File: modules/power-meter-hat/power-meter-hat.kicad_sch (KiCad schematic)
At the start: 14 parts, among them J1 GPIO, U1 CAT24C256

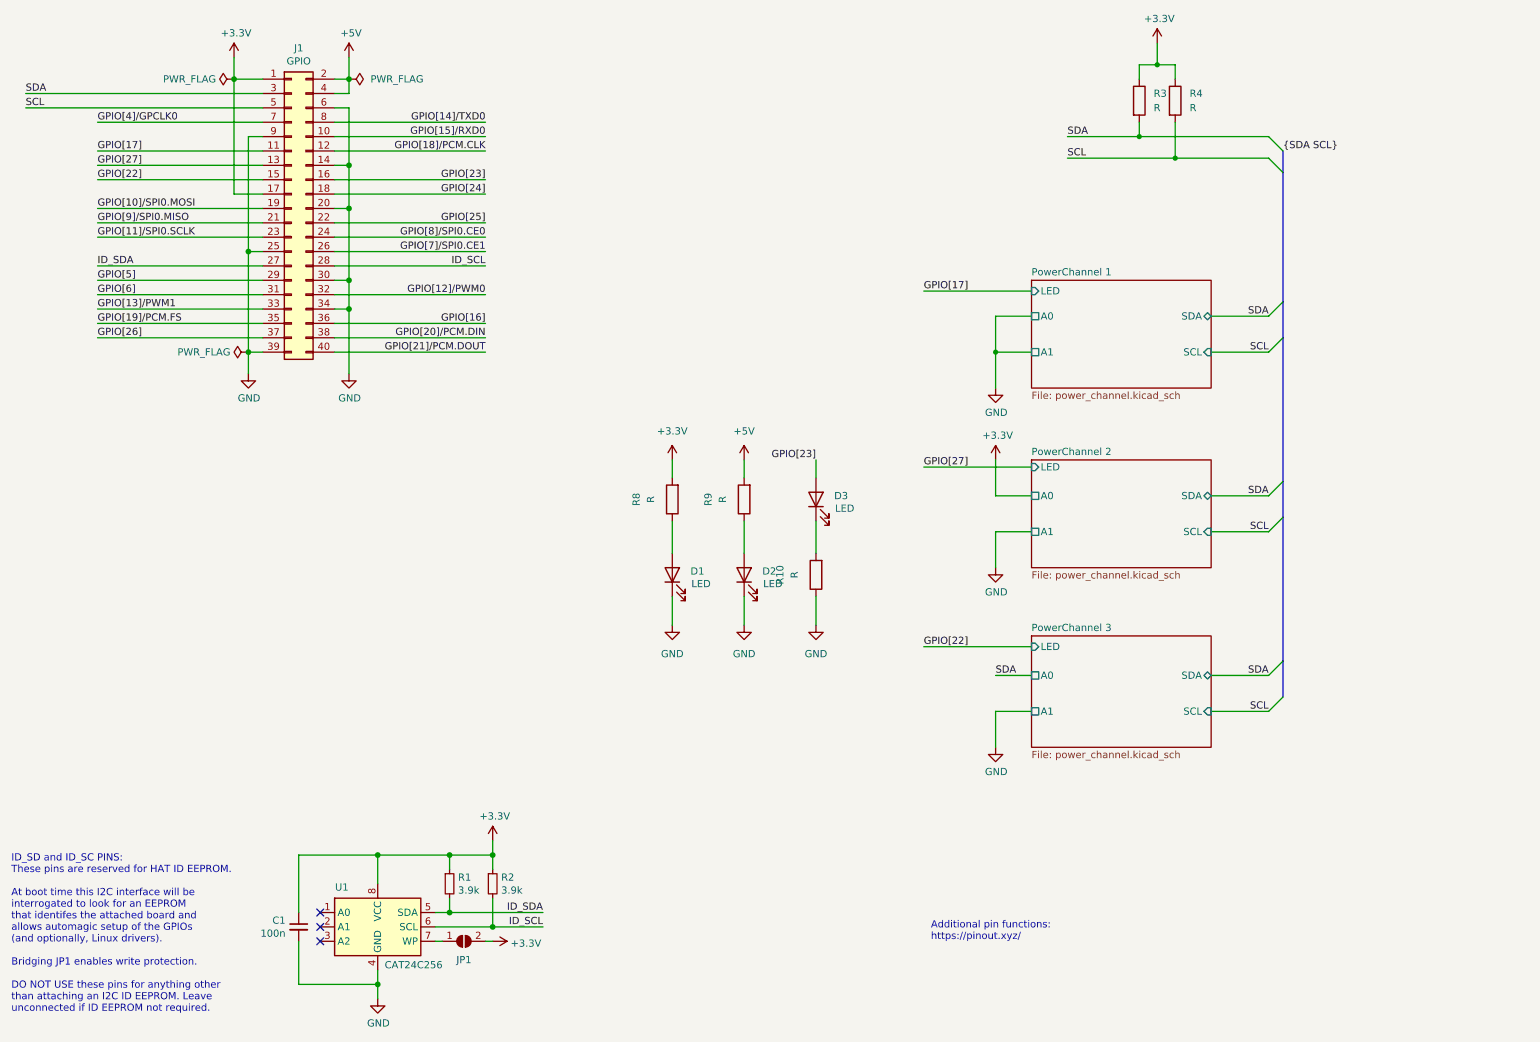
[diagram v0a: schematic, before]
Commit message: Add external power source
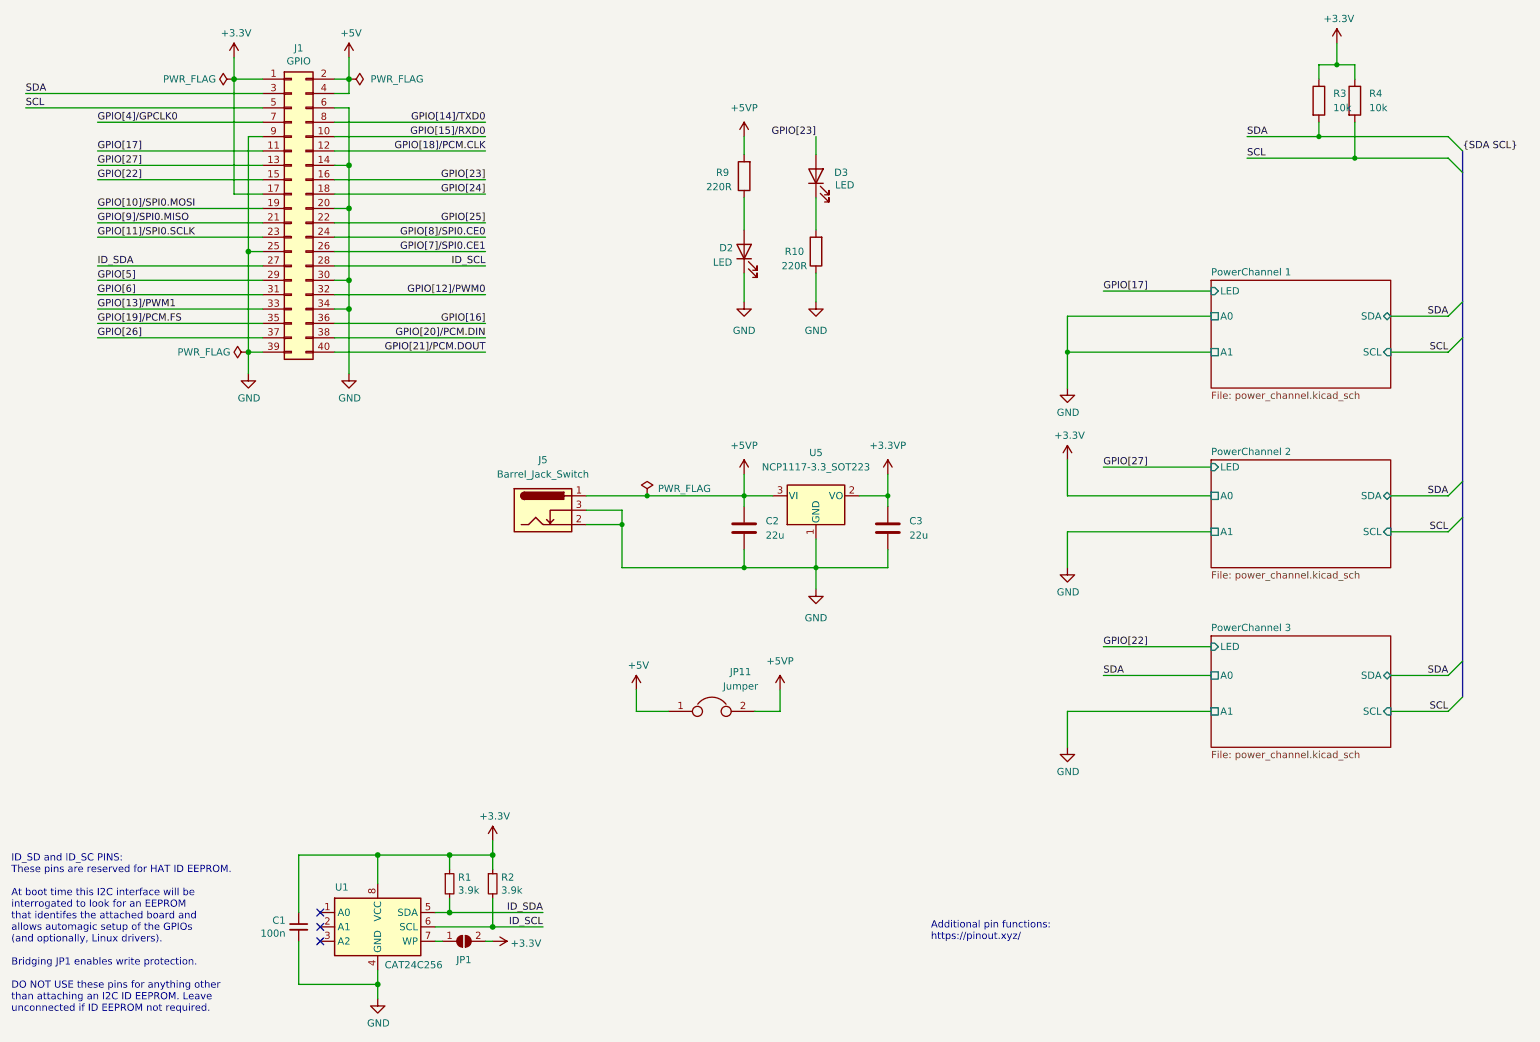
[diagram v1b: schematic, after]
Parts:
- removed D1: LED, LED_SMD:LED_1206_3216Metric_Castellated, symbol Device:LED
- removed R8: R, Resistor_SMD:R_0805_2012Metric_Pad1.20x1.40mm_HandSolder, symbol Device:R
- added C2, C3: 22u, Capacitor_SMD:C_0805_2012Metric_Pad1.18x1.45mm_HandSolder, symbol Device:C
- added J5: Barrel_Jack_Switch, Connector_BarrelJack:BarrelJack_Wuerth_6941xx301002, symbol Connector:Barrel_Jack_Switch
- added JP11: Jumper, Jumper:SolderJumper-2_P1.3mm_Open_TrianglePad1.0x1.5mm, symbol Device:Jumper
- added U5: NCP1117-3.3_SOT223, Package_TO_SOT_SMD:SOT-223-3_TabPin2, symbol Regulator_Linear:NCP1117-3.3_SOT223
- R10, R9: value R -> 220R
- R3, R4: value R -> 10k
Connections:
- net +5V: now also JP11.1; no longer R9.2
- net GND: now also C2.2, C3.2, J5.2, J5.3, U5.1 (GND)
- new net +3.3VP: C3.1, U5.2 (VO)
- new net +5VP: C2.1, J5.1, JP11.2, R9.2, U5.3 (VI)
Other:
- moved on the sheet: D2, D3, R10, R3, R4, R9

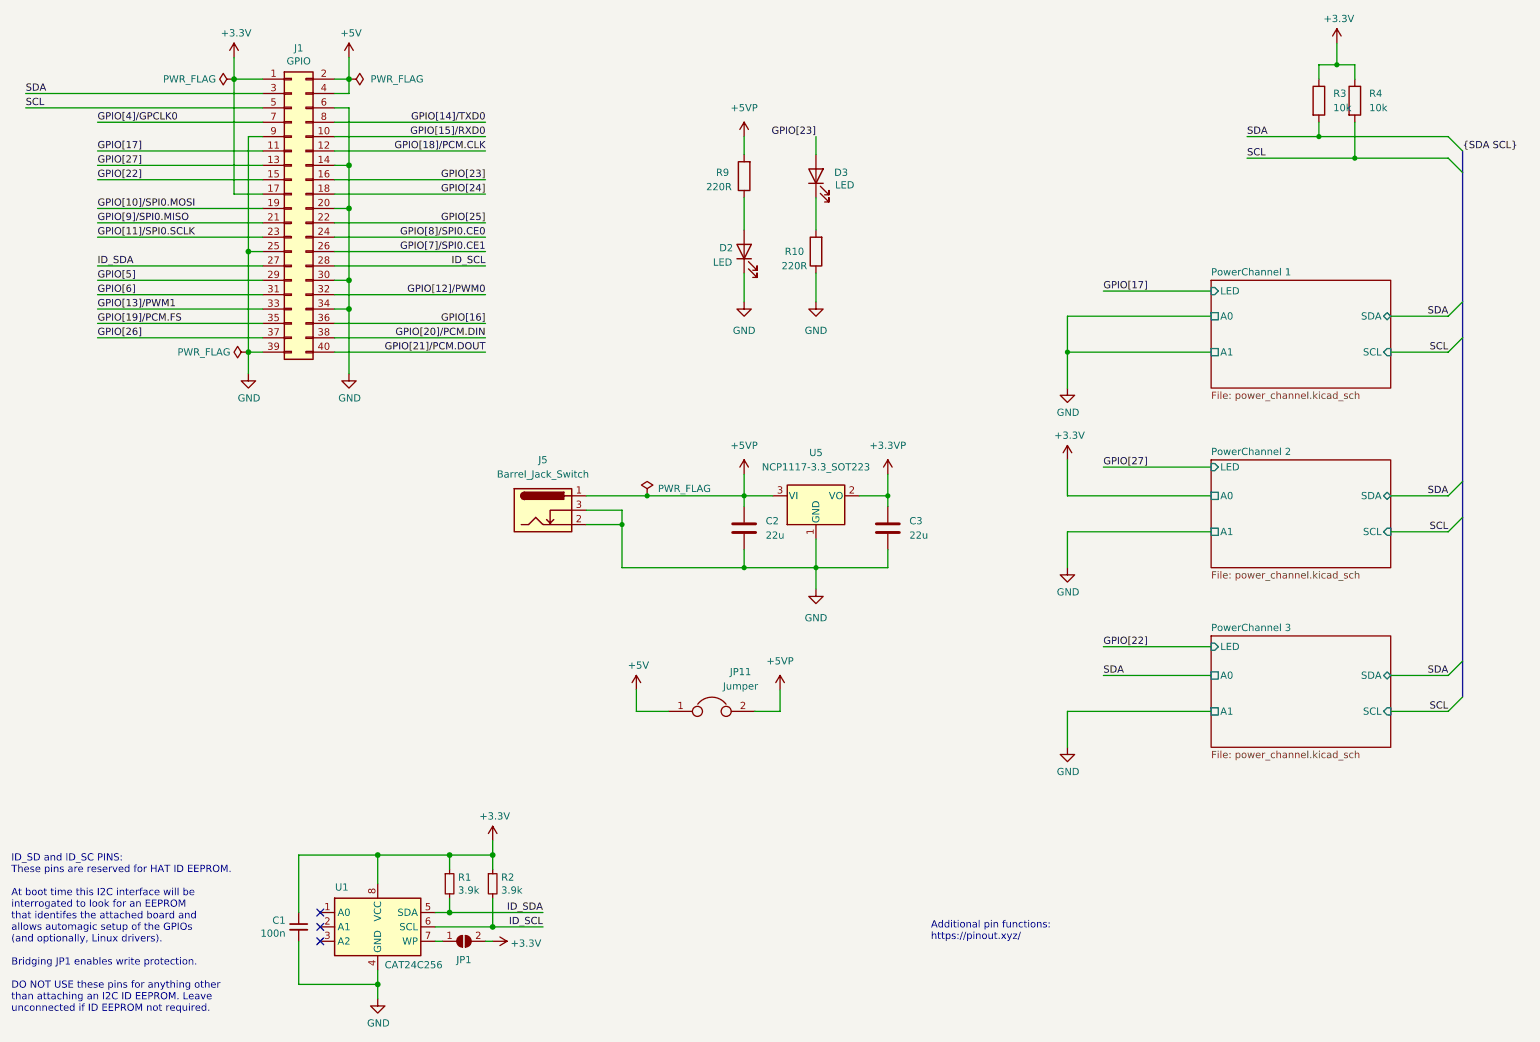
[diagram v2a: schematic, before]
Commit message: Reannotate schematic
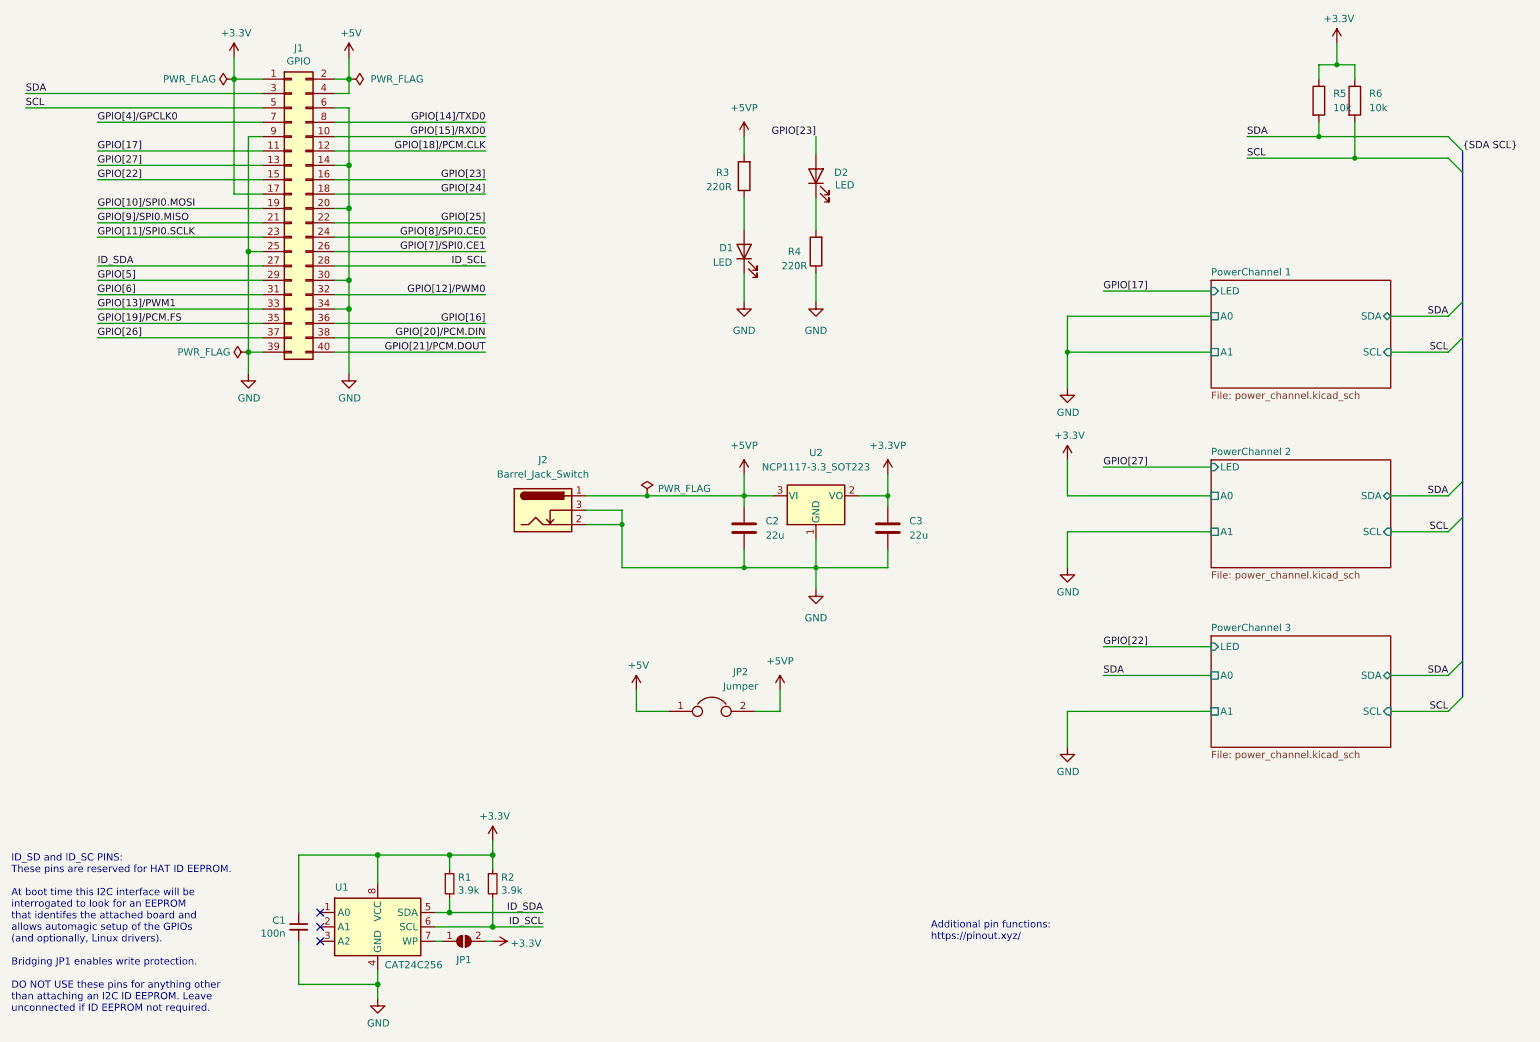
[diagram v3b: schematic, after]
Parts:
- renumbered D2 to D1, D3 to D2, J5 to J2, JP11 to JP2, R9 to R3, R10 to R4, R3 to R5, R4 to R6, U5 to U2

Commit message: Replace barrel jack to CLIFF FC68148
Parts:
- J2: footprint Connector_BarrelJack:BarrelJack_Wuerth_6941xx301002 -> shared_components:BarrelJack_CLIFF_FC68148_Horizontal
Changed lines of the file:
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@@
     (property "Reference" "J2" (id 0) (at 110.49 95.25 0))
     (property "Value" "Barrel_Jack_Switch" (id 1) (at 110.49 97.79 0))
-    (property "Footprint" "Connector_BarrelJack:BarrelJack_Wuerth_6941xx301002" (id 2) (at 111.76 105.156 0)
+    (property "Footprint" "shared_components:BarrelJack_CLIFF_FC68148_Horizontal" (id 2) (at 111.76 105.156 0)
       (effects (font (size 1.27 1.27)) hide)
     )
@@
     )
     (path "/de2dd575-4cac-4804-82f4-2312f850f454"
-      (reference "J2") (unit 1) (value "Barrel_Jack_Switch") (footprint "Connector_BarrelJack:BarrelJack_Wuerth_6941xx301002")
+      (reference "J2") (unit 1) (value "Barrel_Jack_Switch") (footprint "shared_components:BarrelJack_CLIFF_FC68148_Horizontal")
     )
     (path "/7acdcd65-592b-4fae-a99e-c444a4b4e6be/46b0c645-722d-4926-99b1-9a78036c1a17"

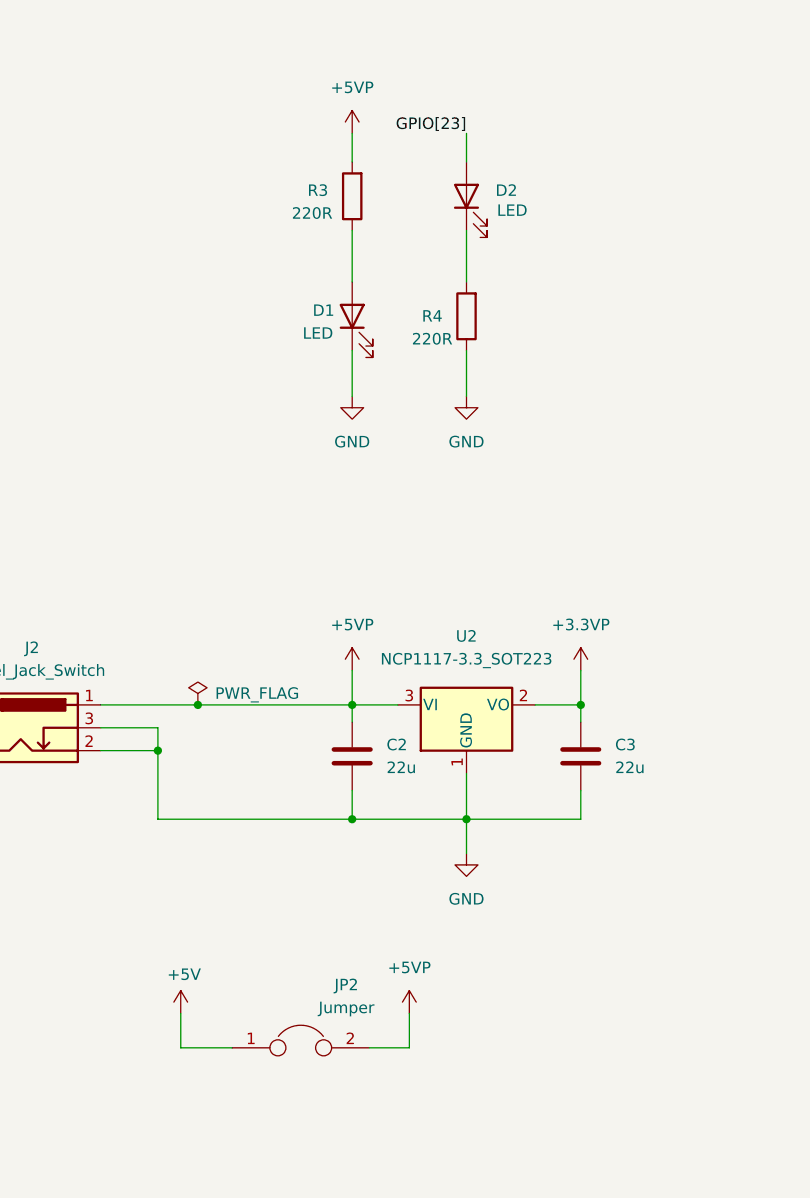
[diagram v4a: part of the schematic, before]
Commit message: Move jumpers to bottom side & other improvements
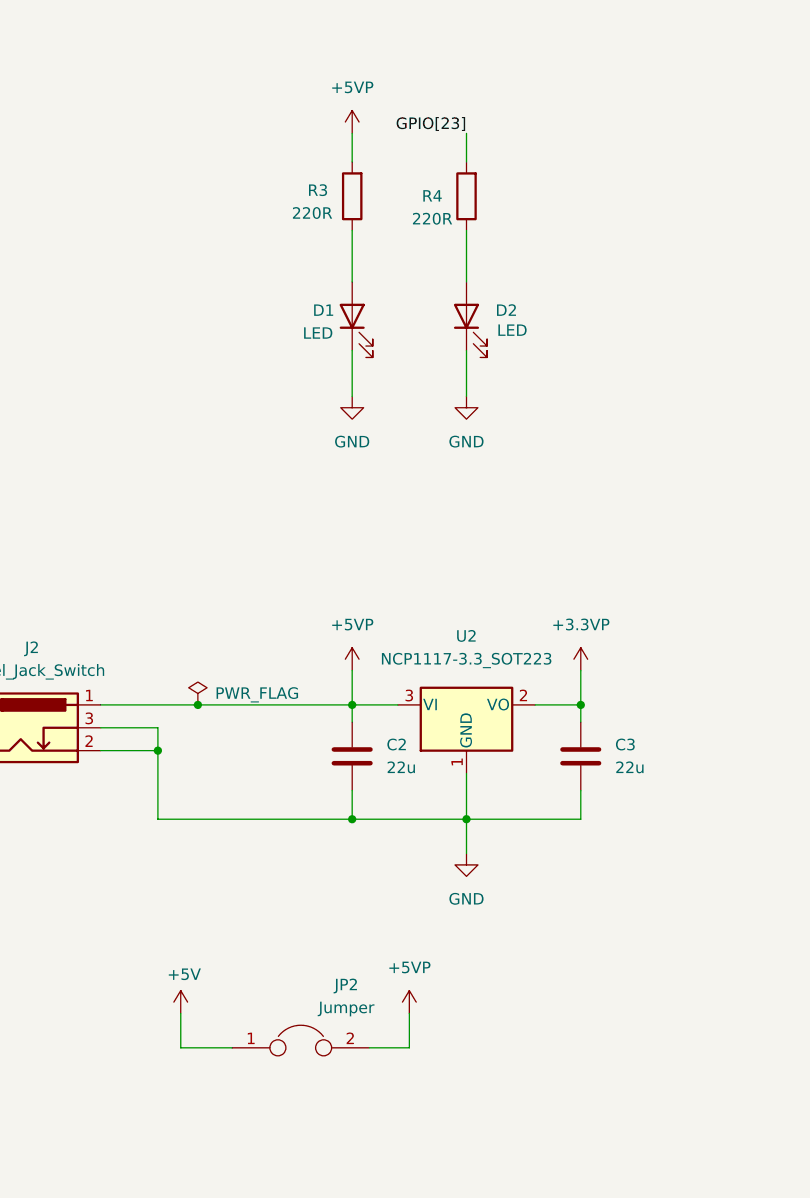
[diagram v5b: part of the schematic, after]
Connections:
- net GND: now also D2.1 (K); no longer R4.1
- net GPIO[23]: now also R4.2; no longer D2.2 (A)
- new net: D2.2 (A), R4.1
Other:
- moved on the sheet: D2, R4
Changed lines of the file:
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@@
     (pin "2")
   )
-  (symbol (lib_id "Device:LED") (at 158.75 45.085 90) (unit 1)
+  (symbol (lib_id "Device:LED") (at 158.75 58.42 90) (unit 1)
     (in_bom yes) (on_board yes)
-    (property "Reference" "D2" (id 0) (at 163.195 44.45 90))
-    (property "Value" "LED" (id 1) (at 163.83 46.6725 90))
-    (property "Footprint" "LED_SMD:LED_1206_3216Metric_Castellated" (id 2) (at 158.75 45.085 0)
+    (property "Reference" "D2" (id 0) (at 163.195 57.785 90))
+    (property "Value" "LED" (id 1) (at 163.83 60.0075 90))
+    (property "Footprint" "LED_SMD:LED_1206_3216Metric_Castellated" (id 2) (at 158.75 58.42 0)
       (effects (font (size 1.27 1.27)) hide)
     )
-    (property "Datasheet" "~" (id 3) (at 158.75 45.085 0)
+    (property "Datasheet" "~" (id 3) (at 158.75 58.42 0)
       (effects (font (size 1.27 1.27)) hide)
     )
@@
     (pin "1")
   )
-  (symbol (lib_id "Device:R") (at 158.75 58.42 180) (unit 1)
+  (symbol (lib_id "Device:R") (at 158.75 45.085 180) (unit 1)
     (in_bom yes) (on_board yes)
-    (property "Reference" "R4" (id 0) (at 154.94 58.42 0))
-    (property "Value" "220R" (id 1) (at 154.94 60.96 0))
-    (property "Footprint" "Resistor_SMD:R_0805_2012Metric_Pad1.20x1.40mm_HandSolder" (id 2) (at 160.528 58.42 90)
+    (property "Reference" "R4" (id 0) (at 154.94 45.085 0))
+    (property "Value" "220R" (id 1) (at 154.94 47.625 0))
+    (property "Footprint" "Resistor_SMD:R_0805_2012Metric_Pad1.20x1.40mm_HandSolder" (id 2) (at 160.528 45.085 90)
       (effects (font (size 1.27 1.27)) hide)
     )
-    (property "Datasheet" "~" (id 3) (at 158.75 58.42 0)
+    (property "Datasheet" "~" (id 3) (at 158.75 45.085 0)
       (effects (font (size 1.27 1.27)) hide)
     )
